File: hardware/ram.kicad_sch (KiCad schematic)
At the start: 33 parts, among them U12 S27KL0641, U4 CCGM1A1

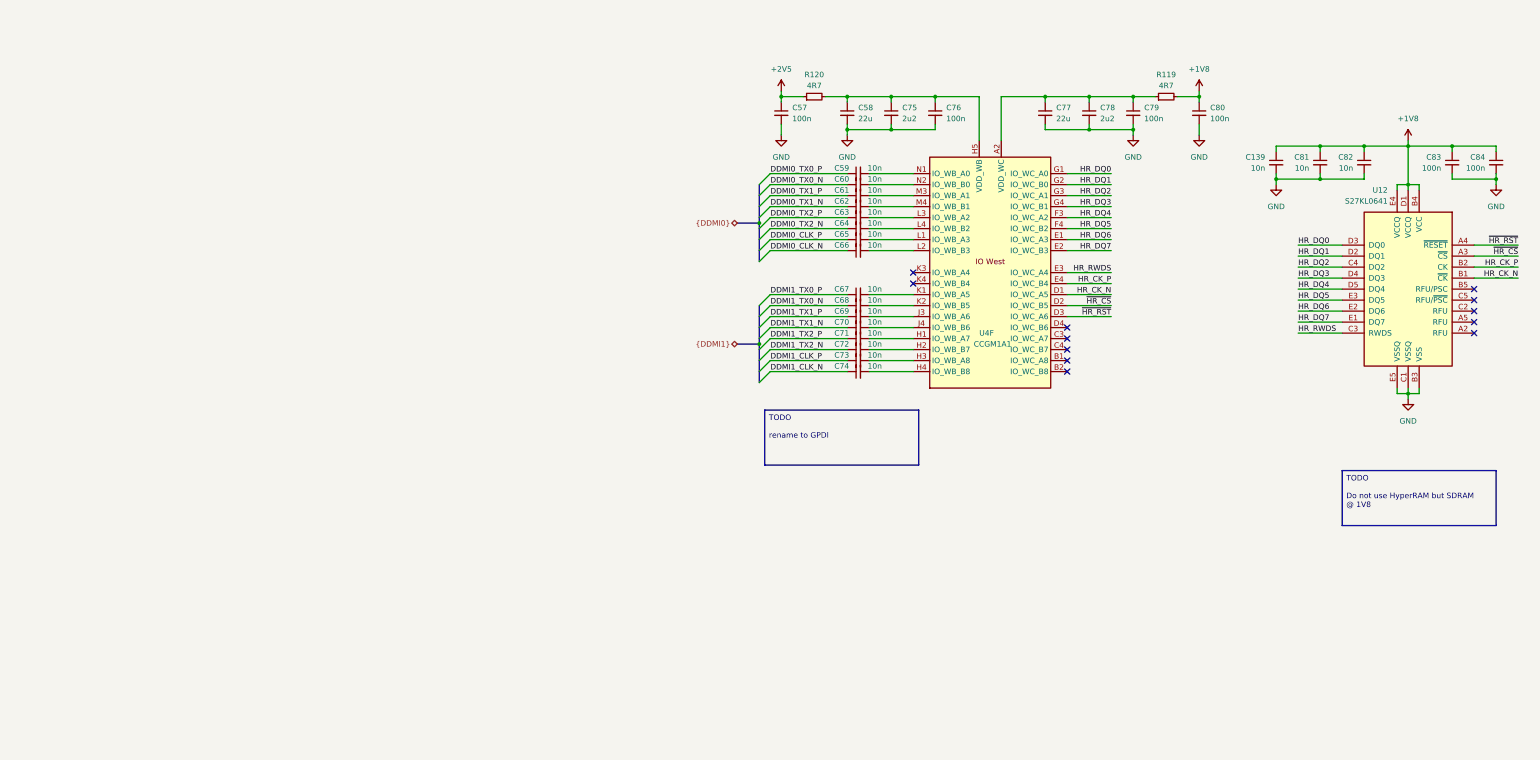
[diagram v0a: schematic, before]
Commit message: Adding SDRAM - missing 3 pins
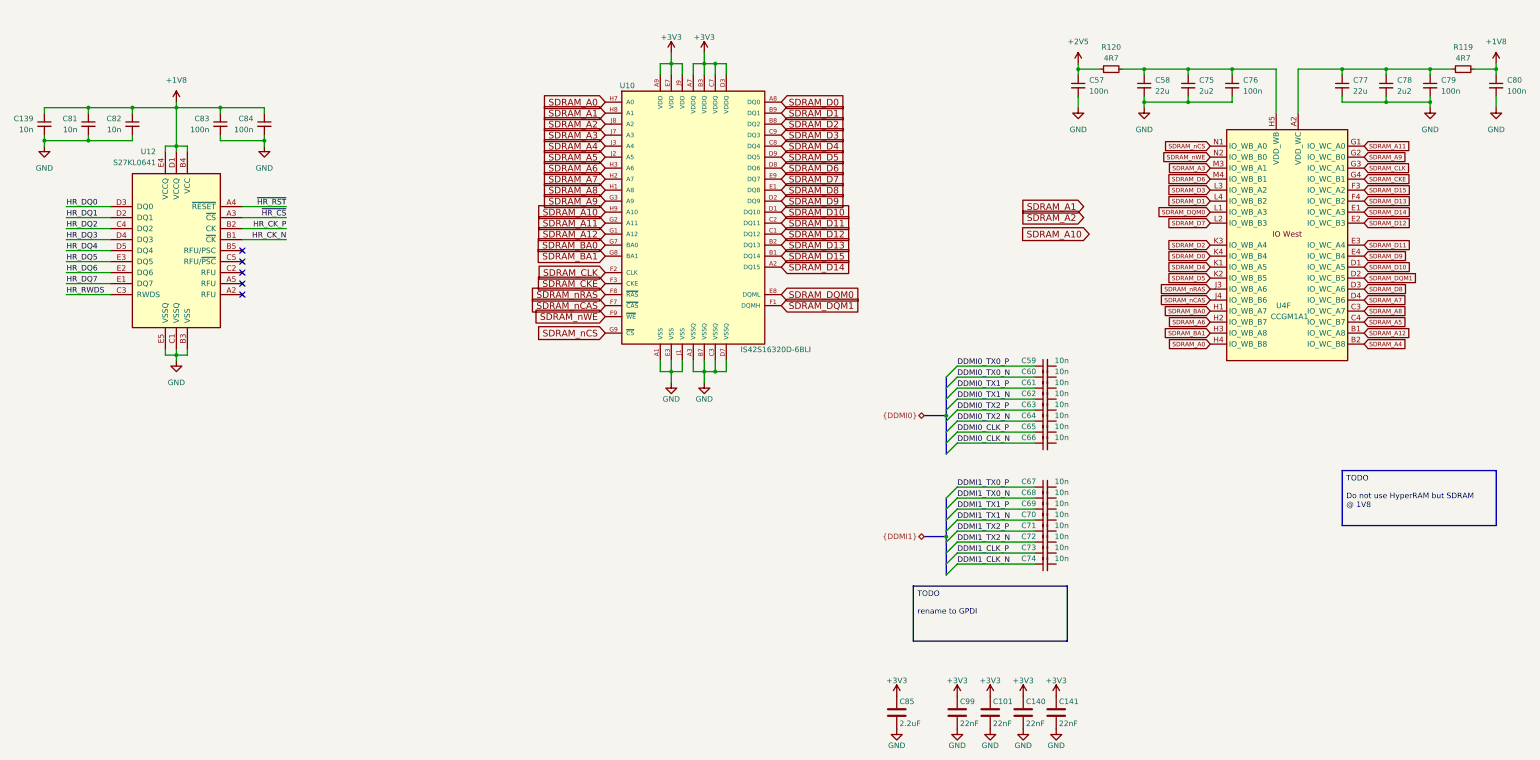
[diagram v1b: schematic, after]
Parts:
- added C101, C140, C99: 22nF, Capacitor_SMD:C_0402_1005Metric, symbol Device:C
- added C141: 22nF, Capacitor_SMD:C_0603_1608Metric, symbol Device:C
- added C85: 2.2uF, Capacitor_SMD:C_0603_1608Metric, symbol Device:C
- added U10: IS42S16320D-6BLI, IS42S16320D:IS42S16320D-6BLI, symbol mt48lc16m16a2tg:IS42S16320D-6BLI
- U12: footprint apparillo-lib:BGA-24_5x5_6.0x8.0mm -> ulx5m-gs:BGA-24_5x5_6.0x8.0mm
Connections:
- net GND: now also C101.2, C140.2, C141.2, C85.2, C99.2, U10.A1 (VSS), U10.A3 (VSSQ), U10.B7 (VSSQ), U10.C3 (VSSQ), U10.D7 (VSSQ), U10.E3 (VSS), U10.J1 (VSS)
- net HR_CK_N: no longer U4.D1 (IO_WC_A5)
- net HR_CK_P: no longer U4.E4 (IO_WC_B4)
- net HR_DQ0: no longer U4.G1 (IO_WC_A0)
- net HR_DQ1: no longer U4.G2 (IO_WC_B0)
- net HR_DQ2: no longer U4.G3 (IO_WC_A1)
- net HR_DQ3: no longer U4.G4 (IO_WC_B1)
- net HR_DQ4: no longer U4.F3 (IO_WC_A2)
- net HR_DQ5: no longer U4.F4 (IO_WC_B2)
- net HR_DQ6: no longer U4.E1 (IO_WC_A3)
- net HR_DQ7: no longer U4.E2 (IO_WC_B3)
- net HR_RWDS: no longer U4.E3 (IO_WC_A4)
- net ~{HR_CS}: no longer U4.D2 (IO_WC_B5)
- net ~{HR_RST}: no longer U4.D3 (IO_WC_A6)
- net at C63.2: no longer U4.L3 (IO_WB_A2)
- net at C69.2: no longer U4.J3 (IO_WB_A6)
- net at C65.2: no longer U4.L1 (IO_WB_A3)
- net at C61.2: no longer U4.M3 (IO_WB_A1)
- net at C70.2: no longer U4.J4 (IO_WB_B6)
- net at C74.2: no longer U4.H4 (IO_WB_B8)
- net at C60.2: no longer U4.N2 (IO_WB_B0)
- net at C73.2: no longer U4.H3 (IO_WB_A8)
- net at C72.2: no longer U4.H2 (IO_WB_B7)
- net SDRAM_A12: now reaches U4.B1 (IO_WC_A8)
- net SDRAM_A12: now also U10.G1 (A12)
- net SDRAM_A4: now reaches U4.B2 (IO_WC_B8)
- net SDRAM_A4: now also U10.J3 (A4)
- net SDRAM_A8: now reaches U4.C3 (IO_WC_A7)
- net SDRAM_A8: now also U10.H1 (A8)
- net SDRAM_A5: now reaches U4.C4 (IO_WC_B7)
- net SDRAM_A5: now also U10.J2 (A5)
- net SDRAM_A7: now reaches U4.D4 (IO_WC_B6)
- net SDRAM_A7: now also U10.H2 (A7)
- net at C71.2: no longer U4.H1 (IO_WB_A7)
- net at C67.2: no longer U4.K1 (IO_WB_A5)
- net at C68.2: no longer U4.K2 (IO_WB_B5)
- net SDRAM_D2: now reaches U4.K3 (IO_WB_A4)
- net SDRAM_D2: now also U10.B8 (DQ2)
- net SDRAM_D0: now reaches U4.K4 (IO_WB_B4)
- net SDRAM_D0: now also U10.A8 (DQ0)
- net at C66.2: no longer U4.L2 (IO_WB_B3)
- net at C64.2: no longer U4.L4 (IO_WB_B2)
- net at C62.2: no longer U4.M4 (IO_WB_B1)
- net at C59.2: no longer U4.N1 (IO_WB_A0)
- new net +3V3: C101.1, C140.1, C141.1, C85.1, C99.1, U10.A7 (VDDQ), U10.A9 (VDD), U10.B3 (VDDQ), U10.C7 (VDDQ), U10.D3 (VDDQ), U10.E7 (VDD), U10.J9 (VDD)
- new net SDRAM_A0: U10.H7 (A0), U4.H4 (IO_WB_B8)
- new net SDRAM_A1: U10.H8 (A1)
- new net SDRAM_A10: U10.H9 (A10)
- new net SDRAM_A11: U10.G2 (A11), U4.G1 (IO_WC_A0)
- new net SDRAM_A2: U10.J8 (A2)
- new net SDRAM_A3: U10.J7 (A3), U4.M3 (IO_WB_A1)
- new net SDRAM_A6: U10.H3 (A6), U4.H2 (IO_WB_B7)
- new net SDRAM_A9: U10.G3 (A9), U4.G2 (IO_WC_B0)
- new net SDRAM_BA0: U10.G7 (BA0), U4.H1 (IO_WB_A7)
- new net SDRAM_BA1: U10.G8 (BA1), U4.H3 (IO_WB_A8)
- new net SDRAM_CKE: U10.F3 (CKE), U4.G4 (IO_WC_B1)
- new net SDRAM_CLK: U10.F2 (CLK), U4.G3 (IO_WC_A1)
- new net SDRAM_D1: U10.B9 (DQ1), U4.L4 (IO_WB_B2)
- new net SDRAM_D10: U10.D1 (DQ10), U4.D1 (IO_WC_A5)
- new net SDRAM_D11: U10.C2 (DQ11), U4.E3 (IO_WC_A4)
- new net SDRAM_D12: U10.C1 (DQ12), U4.E2 (IO_WC_B3)
- new net SDRAM_D13: U10.B2 (DQ13), U4.F4 (IO_WC_B2)
- new net SDRAM_D14: U10.A2 (DQ15), U4.E1 (IO_WC_A3)
- new net SDRAM_D15: U10.B1 (DQ14), U4.F3 (IO_WC_A2)
- new net SDRAM_D3: U10.C9 (DQ3), U4.L3 (IO_WB_A2)
- new net SDRAM_D4: U10.C8 (DQ4), U4.K1 (IO_WB_A5)
- new net SDRAM_D5: U10.D9 (DQ5), U4.K2 (IO_WB_B5)
- new net SDRAM_D6: U10.D8 (DQ6), U4.M4 (IO_WB_B1)
- new net SDRAM_D7: U10.E9 (DQ7), U4.L2 (IO_WB_B3)
- new net SDRAM_D8: U10.E1 (DQ8), U4.D3 (IO_WC_A6)
- new net SDRAM_D9: U10.D2 (DQ9), U4.E4 (IO_WC_B4)
- new net SDRAM_DQM0: U10.E8 (DQML), U4.L1 (IO_WB_A3)
- new net SDRAM_DQM1: U10.F1 (DQMH), U4.D2 (IO_WC_B5)
- new net SDRAM_nCAS: U10.F7 (~{CAS}), U4.J4 (IO_WB_B6)
- new net SDRAM_nCS: U10.G9 (~{CS}), U4.N1 (IO_WB_A0)
- new net SDRAM_nRAS: U10.F8 (~{RAS}), U4.J3 (IO_WB_A6)
- new net SDRAM_nWE: U10.F9 (~{WE}), U4.N2 (IO_WB_B0)
- no-connect marks 12 -> 5
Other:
- moved on the sheet: C139, C57, C58, C59, C60, C61, C62, C63, C64, C65, C66, C67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

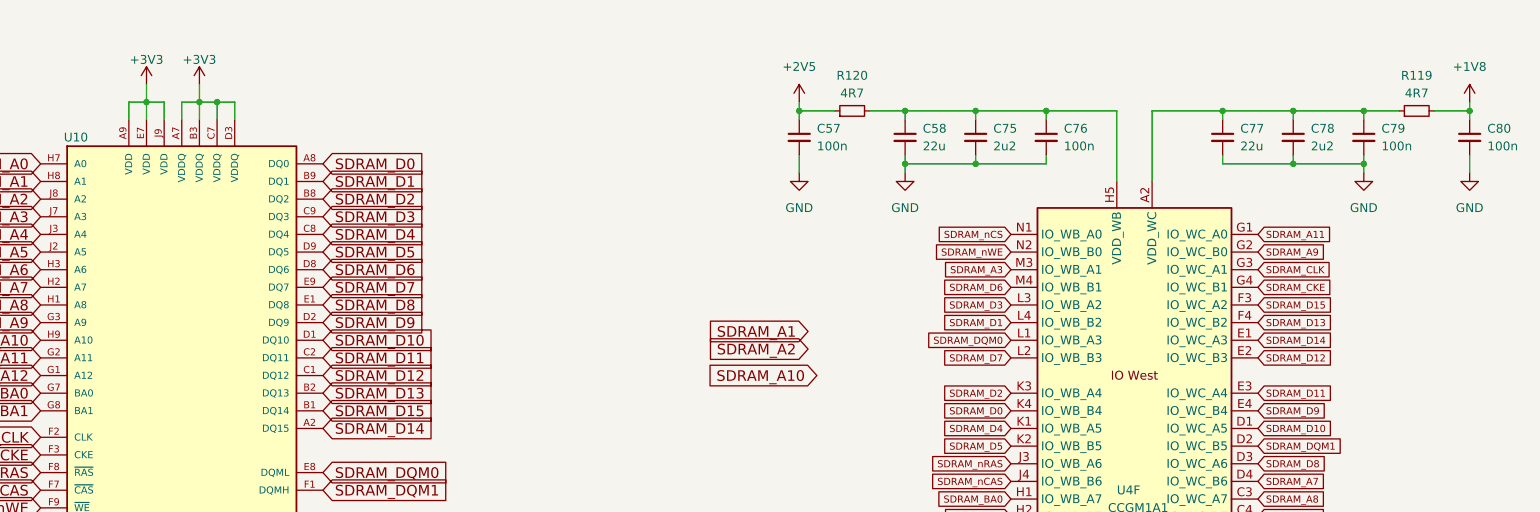
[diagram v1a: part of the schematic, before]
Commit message: Using high SDcard pins for SDRAM
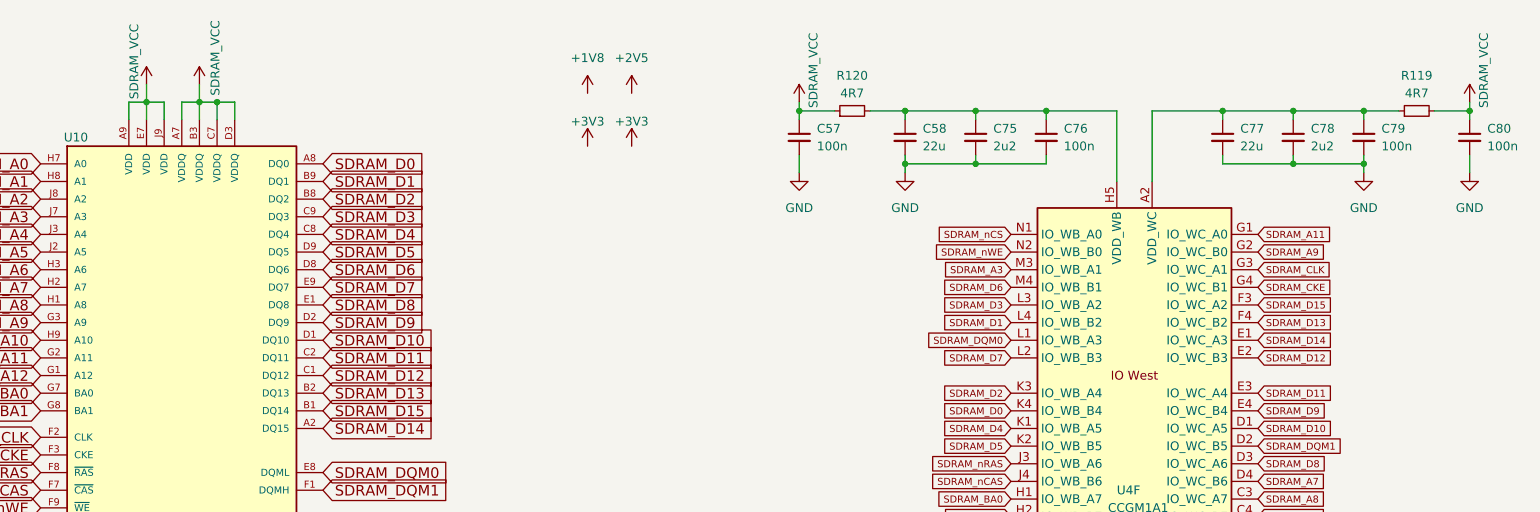
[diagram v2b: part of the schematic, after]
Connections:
- net +1V8: no longer C80.1, R119.2
- net +2V5: no longer C57.1, R120.1
- net +3V3: no longer U10.A7 (VDDQ), U10.A9 (VDD), U10.B3 (VDDQ), U10.C7 (VDDQ), U10.D3 (VDDQ), U10.E7 (VDD), U10.J9 (VDD)
- new net SDRAM_VCC: C57.1, C80.1, R119.2, R120.1, U10.A7 (VDDQ), U10.A9 (VDD), U10.B3 (VDDQ), U10.C7 (VDDQ), U10.D3 (VDDQ), U10.E7 (VDD), U10.J9 (VDD)

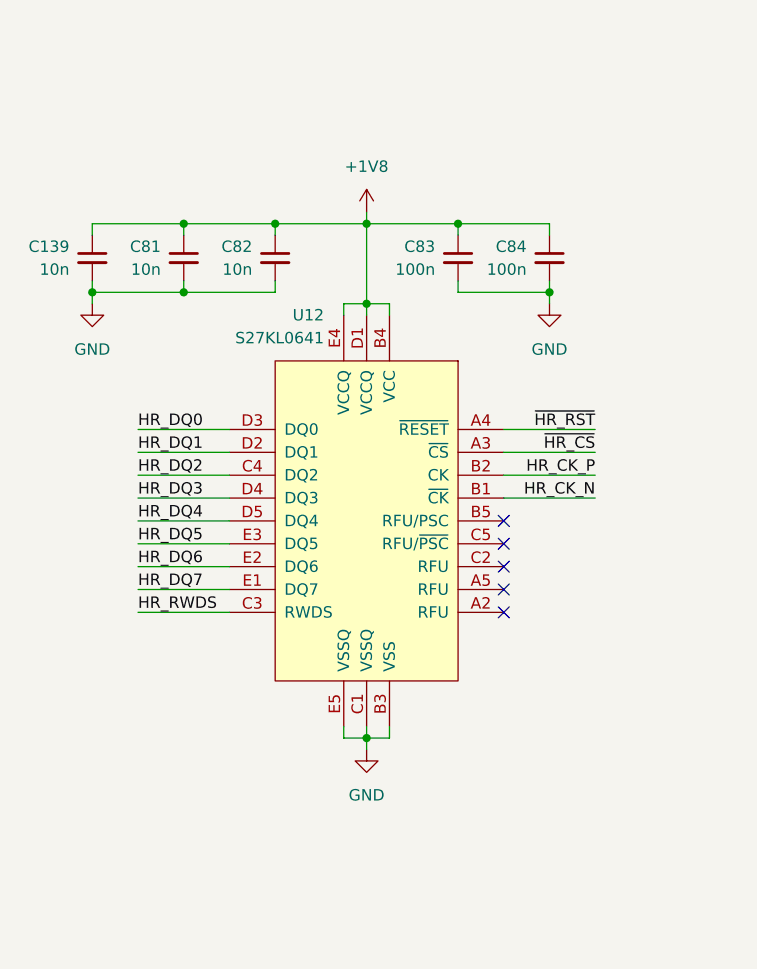
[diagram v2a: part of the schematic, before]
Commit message: PCB - sorting power supplys
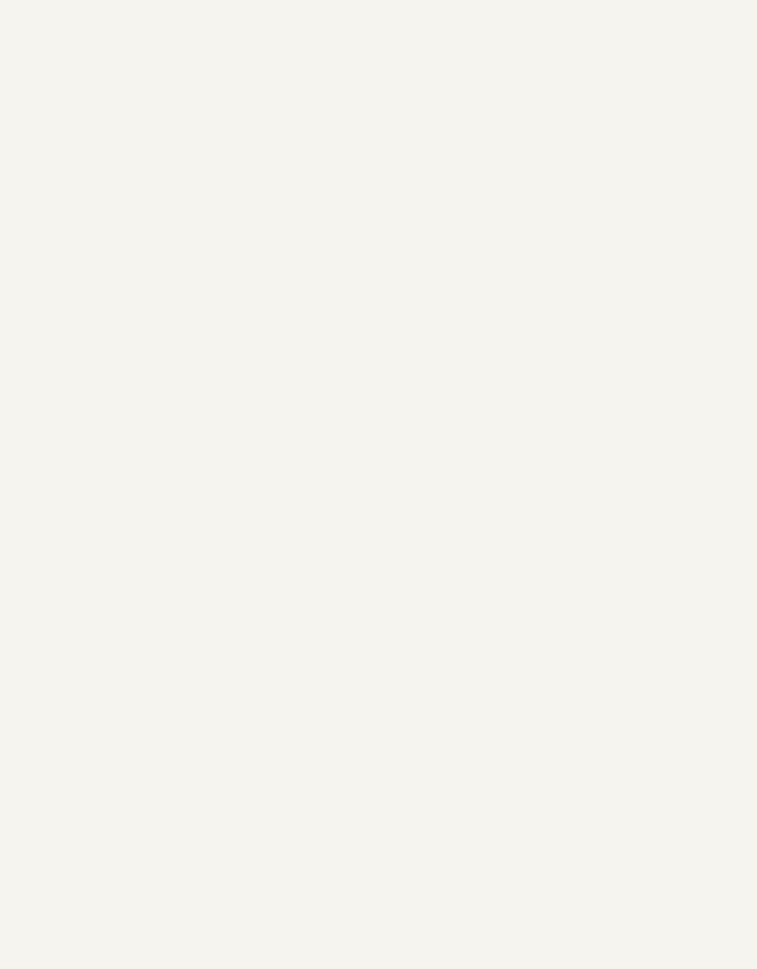
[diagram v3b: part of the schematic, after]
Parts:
- removed C139, C81, C82: 10n, Capacitor_SMD:C_0402_1005Metric, symbol Device:C_Small
- removed C83, C84: 100n, Capacitor_SMD:C_0402_1005Metric, symbol Device:C_Small
- removed U12: S27KL0641, ulx5m-gs:BGA-24_5x5_6.0x8.0mm, symbol HyperRAM:S27KL0641
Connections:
- no-connect marks 5 -> 0

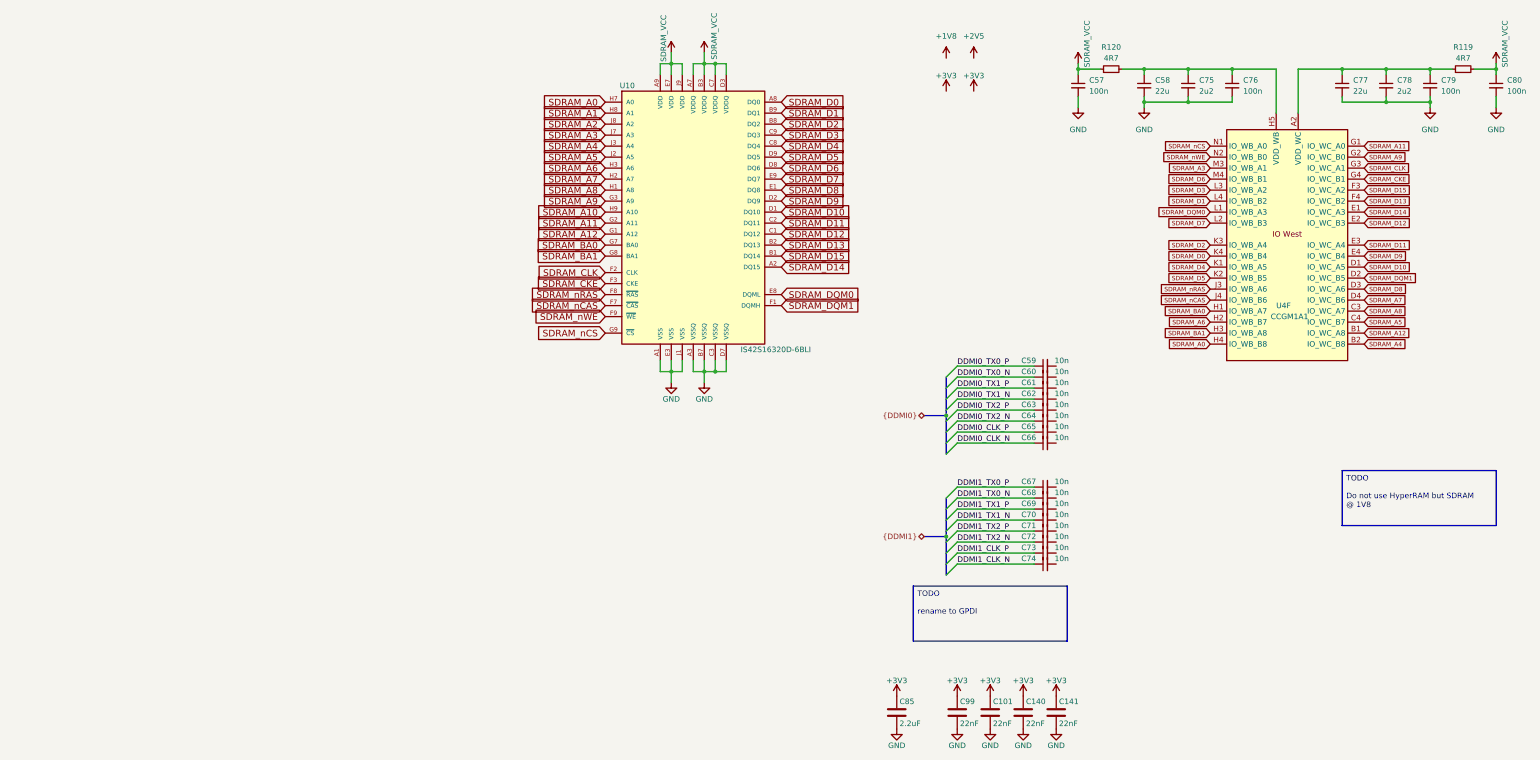
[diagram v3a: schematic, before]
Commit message: Adding USB connector and level converter
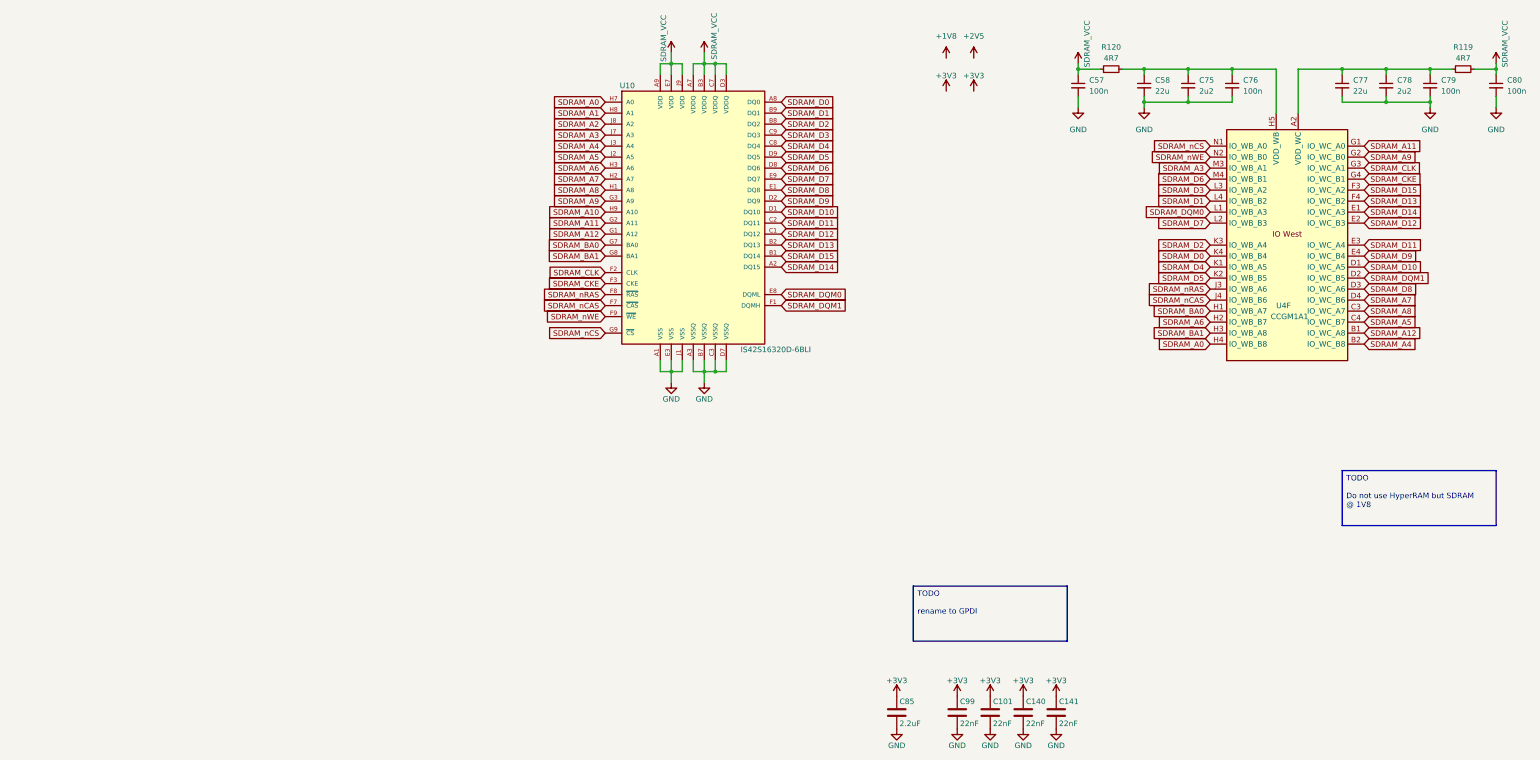
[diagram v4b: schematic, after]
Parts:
- removed C59, C60, C61, C62, C63, C64, C65, C66, C67, C68, C69, C70, C71, C72, C73, C74: 10n, Capacitor_SMD:C_0402_1005Metric, symbol Device:C_Small
- U4: footprint Package_BGA:BGA-324_15.0x15.0mm_Layout18x18_P0.8mm_Ball0.45mm_Pad0.4mm_NSMD -> ulx5m-gs:BGA-324_15.0x15.0mm_Layout18x18_P0.8mm_Ball0.45mm_Pad0.4mm_NSMD

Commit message: Routing diff clock
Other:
- company: (none) -> ${project_creator}
- title: (none) -> ${project_name}
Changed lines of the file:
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@@
 	(generator_version "9.0")
 	(paper "A4")
+	(title_block
+		(title "${project_name}")
+		(date "2025-06-24")
+		(rev "${project_version}")
+		(company "${project_creator}")
+		(comment 1 "${project_license}")
+	)
 	(bus_alias "DDMI0"
 		(members "DDMI0_TX0_P" "DDMI0_TX0_N" "DDMI0_TX1_P" "DDMI0_TX1_N" "DDMI0_TX2_P"

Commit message: Clearing errors
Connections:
- net VCC_WC: now reaches C77.1, C78.1, C79.1, R119.1, U4.A2 (VDD_WC), U4.C2 (VDD_WC), U4.D5 (VDD_WC), U4.F2 (VDD_WC), U4.F5 (VDD_WC)
- net VCC_WB: now reaches C58.1, C75.1, C76.1, R120.2, U4.H5 (VDD_WB), U4.J2 (VDD_WB), U4.K5 (VDD_WB), U4.M2 (VDD_WB), U4.M5 (VDD_WB)
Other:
- moved on the sheet: R119, R120
